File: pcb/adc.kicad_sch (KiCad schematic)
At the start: 19 parts

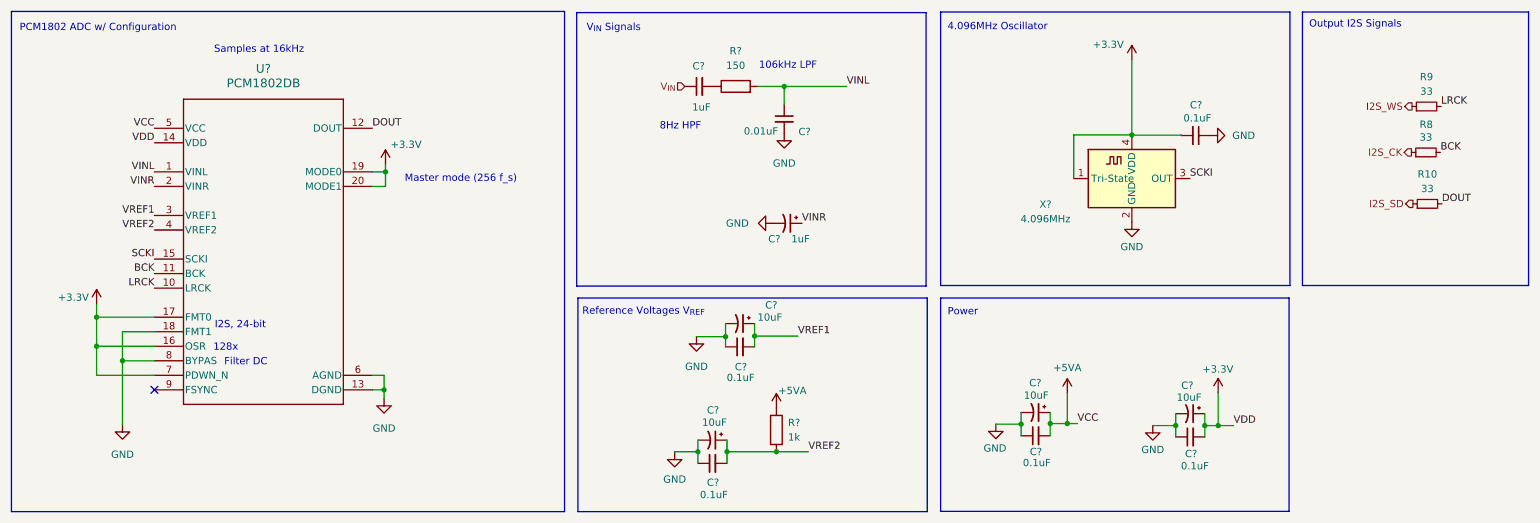
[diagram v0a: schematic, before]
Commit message: ERC fixes
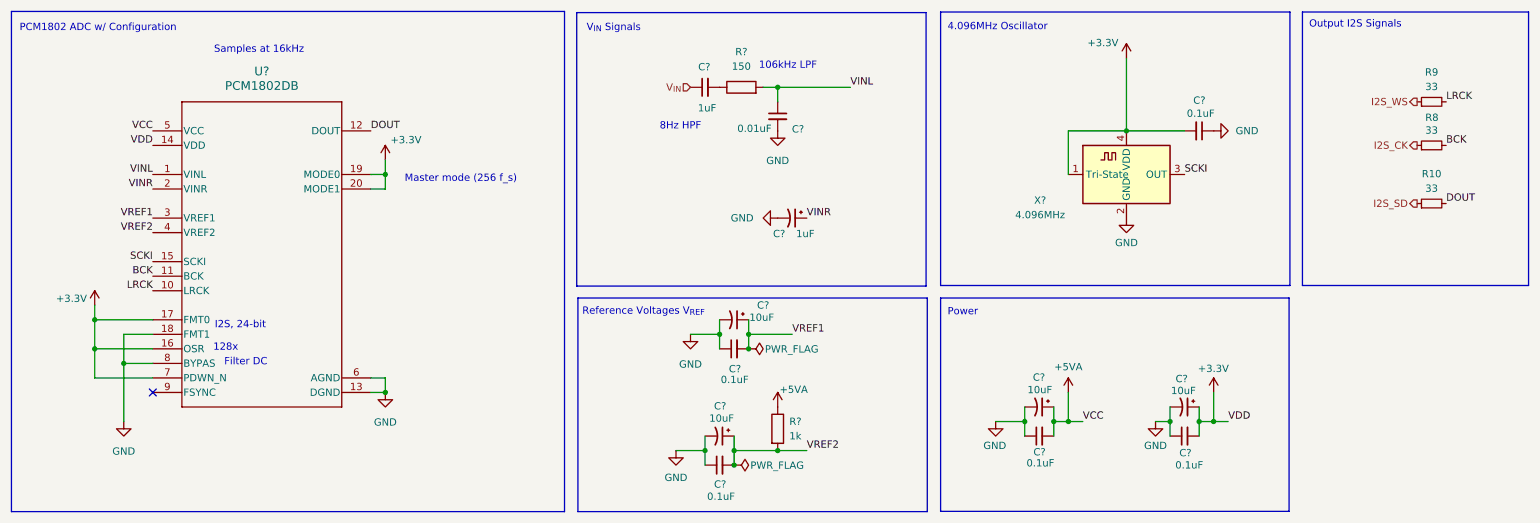
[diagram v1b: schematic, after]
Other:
- moved on the sheet: C?, R10, R8, R9, R?, U?, X?

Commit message: Starting PCB layout
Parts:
- C? (x4): Manufacturer (none) -> KYOCERA AVX
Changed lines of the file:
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@@
+      (effects (font (size 1.27 1.27)) hide)
+    )
+    (property "Manufacturer" "KYOCERA AVX" (at 139.7 127 0)
       (effects (font (size 1.27 1.27)) hide)
     )
@@
       (effects (font (size 1.27 1.27)) hide)
     )
+    (property "Manufacturer" "KYOCERA AVX" (at 195.58 121.92 0)
+      (effects (font (size 1.27 1.27)) hide)
+    )
     (pin "1")
     (pin "2")
@@
       (effects (font (size 1.27 1.27)) hide)
     )
+    (property "Manufacturer" "KYOCERA AVX" (at 142.24 106.68 0)
+      (effects (font (size 1.27 1.27)) hide)
+    )
     (pin "1")
     (pin "2")
@@
       (effects (font (size 1.27 1.27)) hide)
     )
+    (property "Manufacturer" "KYOCERA AVX" (at 220.98 121.92 0)
+      (effects (font (size 1.27 1.27)) hide)
+    )

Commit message: First revision of the pcb layout
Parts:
- C? (x5): footprint Capacitor_SMD:C_1206_3216Metric -> Capacitor_SMD:C_0402_1005Metric; LCSC C577121 -> C1525; MPN CC1206JKNPO9BN104 -> CL05B104KO5NNNC; Manufacturer Yageo -> Samsung Electro-Mechanics
- U?: footprint pcm1802:DB0020A-IPC_A -> Package_SO:SSOP-20_5.3x7.2mm_P0.65mm
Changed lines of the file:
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@@
       (effects (font (size 1.27 1.27)))
     )
-    (property "Footprint" "Capacitor_SMD:C_1206_3216Metric" (at 139.7 132.08 0)
+    (property "Footprint" "Capacitor_SMD:C_0402_1005Metric" (at 139.7 132.08 0)
       (effects (font (size 1.27 1.27)) hide)
     )
@@
       (effects (font (size 1.27 1.27)) hide)
     )
-    (property "LCSC" "C577121" (at 139.7 132.08 0)
-      (effects (font (size 1.27 1.27)) hide)
-    )
-    (property "MPN" "CC1206JKNPO9BN104" (at 139.7 132.08 0)
-      (effects (font (size 1.27 1.27)) hide)
-    )
-    (property "Manufacturer" "Yageo" (at 139.7 132.08 0)
+    (property "LCSC" "C1525" (at 139.7 132.08 0)
+      (effects (font (size 1.27 1.27)) hide)
+    )
+    (property "MPN" "CL05B104KO5NNNC" (at 139.7 132.08 0)
+      (effects (font (size 1.27 1.27)) hide)
+    )
+    (property "Manufacturer" "Samsung Electro-Mechanics" (at 139.7 132.08 0)
       (effects (font (size 1.27 1.27)) hide)
     )
@@
       (effects (font (size 1.27 1.27)))
     )
-    (property "Footprint" "Capacitor_SMD:C_1206_3216Metric" (at 195.58 127 0)
+    (property "Footprint" "Capacitor_SMD:C_0402_1005Metric" (at 195.58 127 0)
       (effects (font (size 1.27 1.27)) hide)
     )
@@
       (effects (font (size 1.27 1.27)) hide)
     )
-    (property "LCSC" "C577121" (at 195.58 127 0)
-      (effects (font (size 1.27 1.27)) hide)
-    )
-    (property "MPN" "CC1206JKNPO9BN104" (at 195.58 127 0)
-      (effects (font (size 1.27 1.27)) hide)
-    )
-    (property "Manufacturer" "Yageo" (at 195.58 127 0)
+    (property "LCSC" "C1525" (at 195.58 127 0)
+      (effects (font (size 1.27 1.27)) hide)
+    )
+    (property "MPN" "CL05B104KO5NNNC" (at 195.58 127 0)
+      (effects (font (size 1.27 1.27)) hide)
+    )
+    (property "Manufacturer" "Samsung Electro-Mechanics" (at 195.58 127 0)
       (effects (font (size 1.27 1.27)) hide)
     )
@@
       (effects (font (size 1.27 1.27)))
     )
-    (property "Footprint" "Capacitor_SMD:C_1206_3216Metric" (at 142.24 111.76 0)
+    (property "Footprint" "Capacitor_SMD:C_0402_1005Metric" (at 142.24 111.76 0)
       (effects (font (size 1.27 1.27)) hide)
     )
@@
       (effects (font (size 1.27 1.27)) hide)
     )
-    (property "LCSC" "C577121" (at 142.24 111.76 0)
-      (effects (font (size 1.27 1.27)) hide)
-    )
-    (property "MPN" "CC1206JKNPO9BN104" (at 142.24 111.76 0)
-      (effects (font (size 1.27 1.27)) hide)
-    )
-    (property "Manufacturer" "Yageo" (at 142.24 111.76 0)
+    (property "LCSC" "C1525" (at 142.24 111.76 0)
+      (effects (font (size 1.27 1.27)) hide)
+    )
+    (property "MPN" "CL05B104KO5NNNC" (at 142.24 111.76 0)
+      (effects (font (size 1.27 1.27)) hide)
+    )
+    (property "Manufacturer" "Samsung Electro-Mechanics" (at 142.24 111.76 0)
       (effects (font (size 1.27 1.27)) hide)
     )
@@
       (effects (font (size 1.524 1.524)))
     )
-    (property "Footprint" "pcm1802:DB0020A-IPC_A" (at 40.64 73.66 0)
+    (property "Footprint" "Package_SO:SSOP-20_5.3x7.2mm_P0.65mm" (at 40.64 73.66 0)
       (effects (font (size 1.27 1.27) italic) hide)
     )
@@
       (effects (font (size 1.27 1.27)))
     )
-    (property "Footprint" "Capacitor_SMD:C_1206_3216Metric" (at 220.98 127 0)
+    (property "Footprint" "Capacitor_SMD:C_0402_1005Metric" (at 220.98 127 0)
       (effects (font (size 1.27 1.27)) hide)
     )
@@
       (effects (font (size 1.27 1.27)) hide)
     )
-    (property "LCSC" "C577121" (at 220.98 127 0)
-      (effects (font (size 1.27 1.27)) hide)
-    )
-    (property "MPN" "CC1206JKNPO9BN104" (at 220.98 127 0)
-      (effects (font (size 1.27 1.27)) hide)
-    )
-    (property "Manufacturer" "Yageo" (at 220.98 127 0)
+    (property "LCSC" "C1525" (at 220.98 127 0)
+      (effects (font (size 1.27 1.27)) hide)
+    )
+    (property "MPN" "CL05B104KO5NNNC" (at 220.98 127 0)
+      (effects (font (size 1.27 1.27)) hide)
+    )
+    (property "Manufacturer" "Samsung Electro-Mechanics" (at 220.98 127 0)
       (effects (font (size 1.27 1.27)) hide)
     )
@@
       (effects (font (size 1.27 1.27)))
     )
-    (property "Footprint" "Capacitor_SMD:C_1206_3216Metric" (at 223.52 73.66 0)
+    (property "Footprint" "Capacitor_SMD:C_0402_1005Metric" (at 223.52 73.66 0)
       (effects (font (size 1.27 1.27)) hide)
     )
@@
       (effects (font (size 1.27 1.27)) hide)
     )
-    (property "LCSC" "C577121" (at 223.52 73.66 0)
-      (effects (font (size 1.27 1.27)) hide)
-    )
-    (property "MPN" "CC1206JKNPO9BN104" (at 223.52 73.66 0)
-      (effects (font (size 1.27 1.27)) hide)
-    )
-    (property "Manufacturer" "Yageo" (at 223.52 73.66 0)
-      (effects (font (size 1.27 1.27)) hide)
-    )
+    (property "LCSC" "C1525" (at 223.52 73.66 0)
+      (effects (font (size 1.27 1.27)) hide)
+    )
+    (property "MPN" "CL05B104KO5NNNC" (at 223.52 73.66 0)
+      (effects (font (size 1.27 1.27)) hide)
+    )
+    (property "Manufacturer" "Samsung Electro-Mechanics" (at 223.52 73.66 0)
+      (effects (font (size 1.27 1.27)) hide)
+    )
